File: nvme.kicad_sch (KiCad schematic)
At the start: 18 parts, among them J4 Bus_M.2_Socket_M, U7 ASEK-32.768KHZ-L-R-T, U8 AP3441SHE-7B

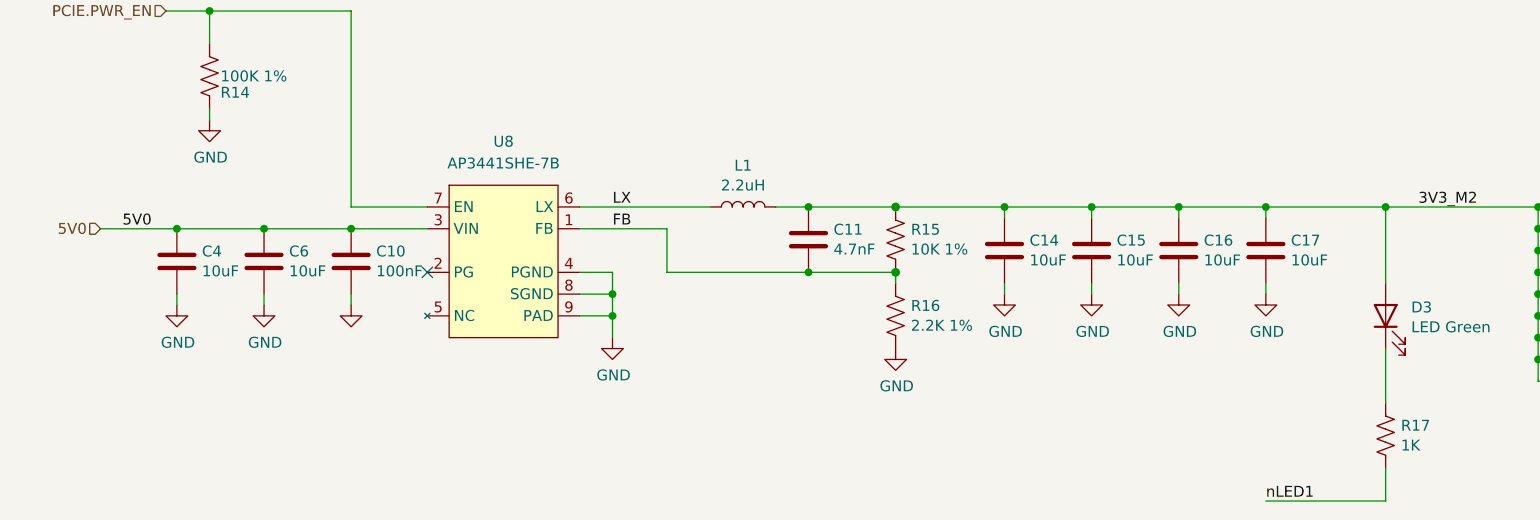
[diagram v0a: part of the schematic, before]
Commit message: restructured symbols, added footprints
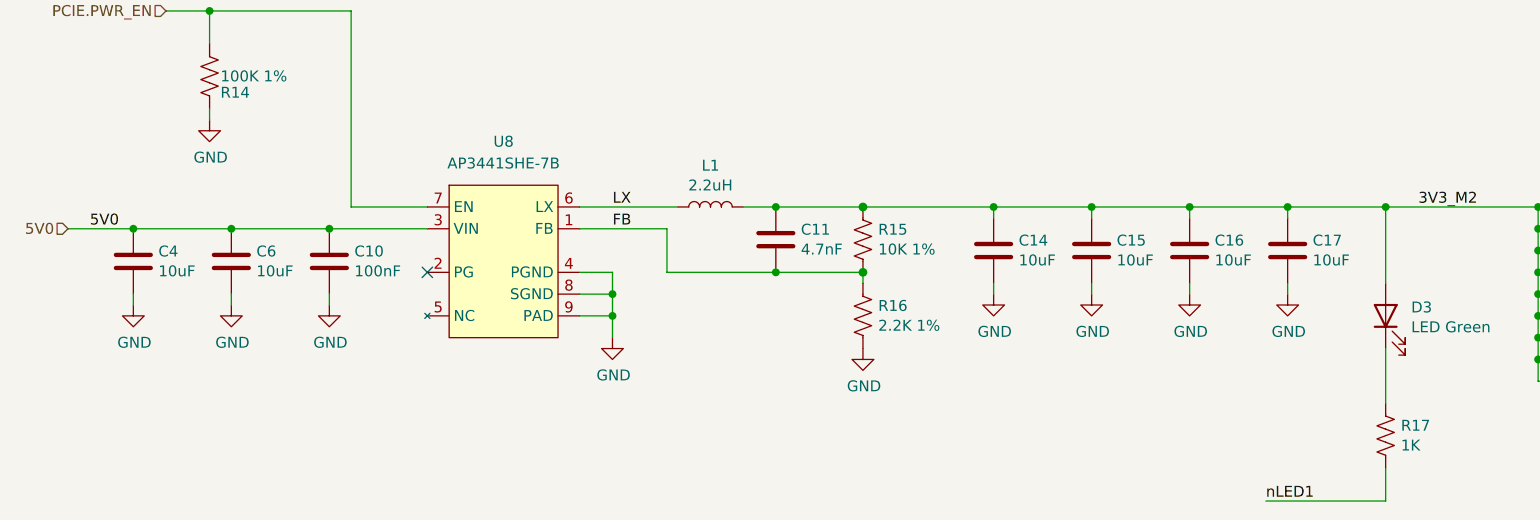
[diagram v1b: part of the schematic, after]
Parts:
- C10, C11, C14, C15, C16, C17, C19, C4, C6: symbol Device:C -> library:C
- D3: symbol Device:LED -> library:LED
- J4: symbol CM5IO:Bus_M.2_Socket_M -> library:Bus_M.2_Socket_M
- L1: symbol Device:L -> library:L
- R14, R15, R16, R17: symbol Device:R_US -> library:R_US
- U7: symbol CM5IO:ASEK-32.768KHZ-L-R-T -> library:ASEK-32.768KHZ-L-R-T
- U8: symbol CM5IO:AP3441SHE-7B -> library:AP3441SHE-7B
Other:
- moved on the sheet: C10, C11, C14, C16, C17, C4, C6, L1, R15, R16

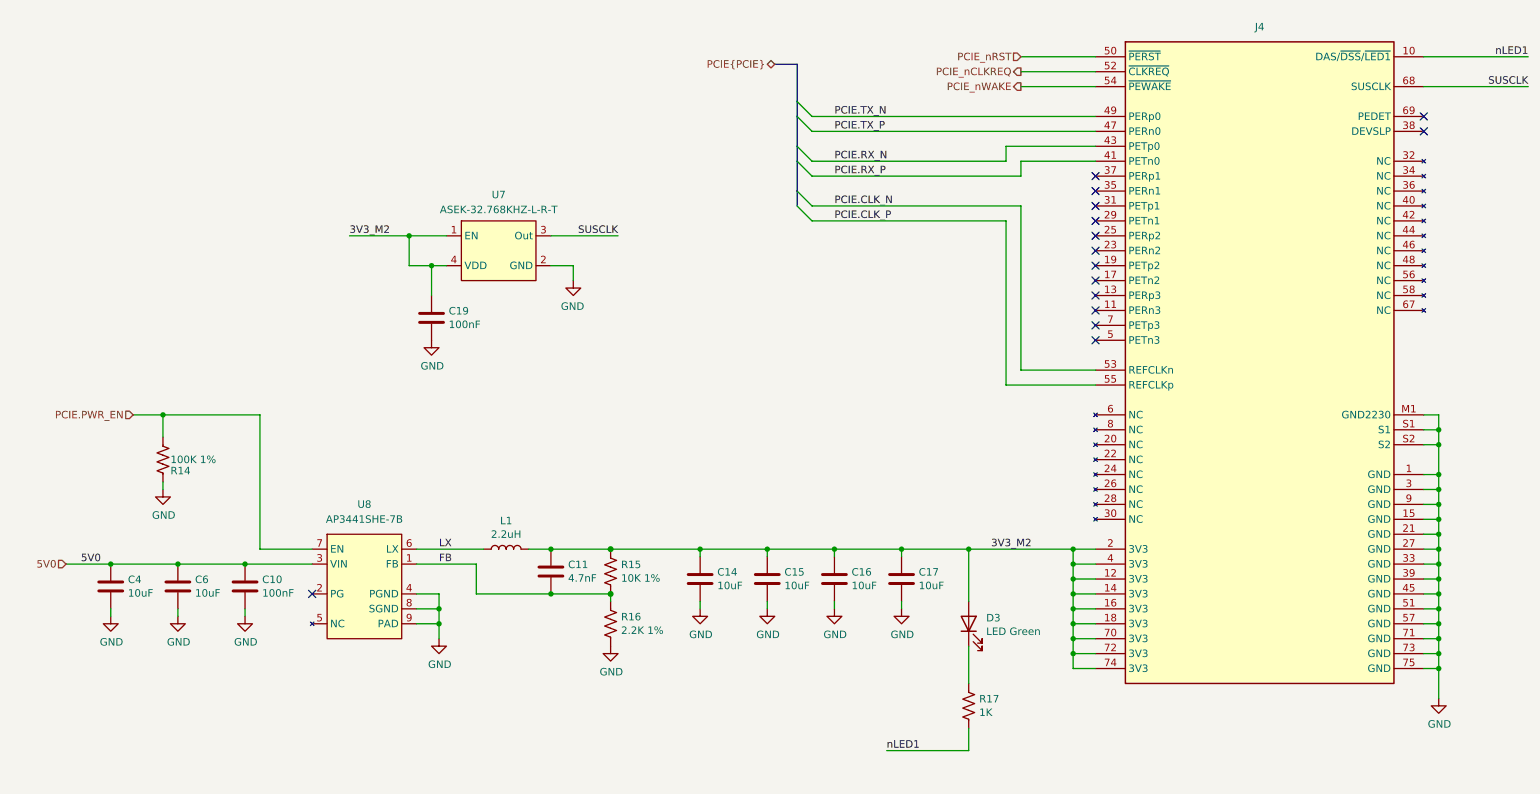
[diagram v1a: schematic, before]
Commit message: added second camera, 6-axis imu
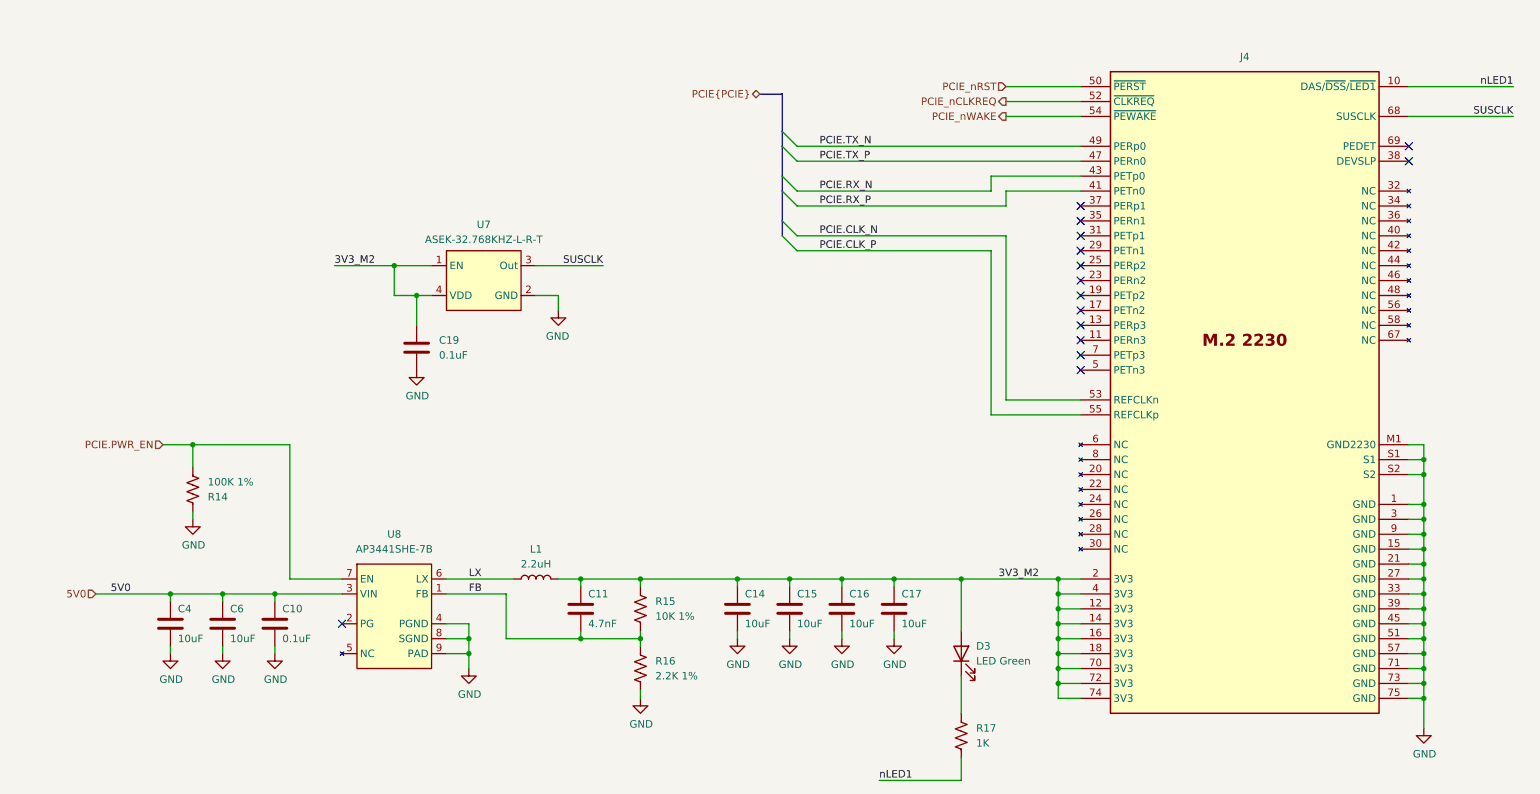
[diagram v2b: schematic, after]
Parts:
- C10, C19: value 100nF -> 0.1uF
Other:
- moved on the sheet: C10, C11, C14, C15, C16, C17, C19, C4, C6, D3, L1, R14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

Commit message: annotations, small fixes
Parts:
- renumbered C19 to C1, C11 to C2, C14 to C3, C15 to C4, C16 to C5, C17 to C6, C4 to C7, C6 to C8, C10 to C9, J4 to J3, R14 to R5, R15 to R6, R16 to R7, R17 to R8, U7 to U1, U8 to U2
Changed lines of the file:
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@@
 		(on_board yes)
 		(dnp no)
-		(property "Reference" "C16"
+		(property "Reference" "C5"
 			(at 157.48 123.19 0)
 			(effects
@@
 			(project "CUTIE-CITRUS"
 				(path "/40af415e-5e3a-41a5-ab07-08c2181863e4/7953df6c-8185-4fff-8cd2-b6d3791adbaa"
-					(reference "C16")
+					(reference "C5")
 					(unit 1)
 				)
@@
 		(on_board yes)
 		(dnp no)
-		(property "Reference" "#PWR018"
+		(property "Reference" "#PWR012"
 			(at 156.21 137.16 0)
 			(effects
@@
 			(project "CUTIE-CITRUS"
 				(path "/40af415e-5e3a-41a5-ab07-08c2181863e4/7953df6c-8185-4fff-8cd2-b6d3791adbaa"
-					(reference "#PWR018")
+					(reference "#PWR012")
 					(unit 1)
 				)
@@
 		(on_board yes)
 		(dnp no)
-		(property "Reference" "C6"
+		(property "Reference" "C8"
 			(at 52.07 125.73 0)
 			(effects
@@
 			(project "CUTIE-CITRUS"
 				(path "/40af415e-5e3a-41a5-ab07-08c2181863e4/7953df6c-8185-4fff-8cd2-b6d3791adbaa"
-					(reference "C6")
+					(reference "C8")
 					(unit 1)
 				)
@@
 		(on_board yes)
 		(dnp no)
-		(property "Reference" "#PWR021"
+		(property "Reference" "#PWR015"
 			(at 50.8 139.7 0)
 			(effects
@@
 			(project "CUTIE-CITRUS"
 				(path "/40af415e-5e3a-41a5-ab07-08c2181863e4/7953df6c-8185-4fff-8cd2-b6d3791adbaa"
-					(reference "#PWR021")
+					(reference "#PWR015")
 					(unit 1)
 				)
@@
 		(on_board yes)
 		(dnp no)
-		(property "Reference" "#PWR03"
+		(property "Reference" "#PWR019"
 			(at 255.27 152.4 0)
 			(effects
@@
 			(project "CUTIE-CITRUS"
 				(path "/40af415e-5e3a-41a5-ab07-08c2181863e4/7953df6c-8185-4fff-8cd2-b6d3791adbaa"
-					(reference "#PWR03")
+					(reference "#PWR019")
 					(unit 1)
 				)
@@
 		(on_board yes)
 		(dnp no)
-		(property "Reference" "#PWR024"
+		(property "Reference" "#PWR013"
 			(at 165.1 137.16 0)
 			(effects
@@
 			(project "CUTIE-CITRUS"
 				(path "/40af415e-5e3a-41a5-ab07-08c2181863e4/7953df6c-8185-4fff-8cd2-b6d3791adbaa"
-					(reference "#PWR024")
+					(reference "#PWR013")
 					(unit 1)
 				)
@@
 		(on_board yes)
 		(dnp no)
-		(property "Reference" "R17"
+		(property "Reference" "R8"
 			(at 179.07 146.05 0)
 			(effects
@@
 			(project "CUTIE-CITRUS"
 				(path "/40af415e-5e3a-41a5-ab07-08c2181863e4/7953df6c-8185-4fff-8cd2-b6d3791adbaa"
-					(reference "R17")
+					(reference "R8")
 					(unit 1)
 				)
@@
 		(on_board yes)
 		(dnp no)
-		(property "Reference" "R15"
+		(property "Reference" "R6"
 			(at 124.46 124.46 0)
 			(effects
@@
 			(project "CUTIE-CITRUS"
 				(path "/40af415e-5e3a-41a5-ab07-08c2181863e4/7953df6c-8185-4fff-8cd2-b6d3791adbaa"
-					(reference "R15")
+					(reference "R6")
 					(unit 1)
 				)
@@
 		(on_board yes)
 		(dnp no)
-		(property "Reference" "C19"
+		(property "Reference" "C1"
 			(at 87.63 80.01 0)
 			(effects
@@
 			(project "CUTIE-CITRUS"
 				(path "/40af415e-5e3a-41a5-ab07-08c2181863e4/7953df6c-8185-4fff-8cd2-b6d3791adbaa"
-					(reference "C19")
+					(reference "C1")
 					(unit 1)
 				)
@@
 		(on_board yes)
 		(dnp no)
-		(property "Reference" "R14"
+		(property "Reference" "R5"
 			(at 48.26 106.68 0)
 			(effects
@@
 			(project "CUTIE-CITRUS"
 				(path "/40af415e-5e3a-41a5-ab07-08c2181863e4/7953df6c-8185-4fff-8cd2-b6d3791adbaa"
-					(reference "R14")
+					(reference "R5")
 					(unit 1)
 				)
@@
 		(on_board yes)
 		(dnp no)
-		(property "Reference" "R16"
+		(property "Reference" "R7"
 			(at 124.46 134.62 0)
 			(effects
@@
 			(project "CUTIE-CITRUS"
 				(path "/40af415e-5e3a-41a5-ab07-08c2181863e4/7953df6c-8185-4fff-8cd2-b6d3791adbaa"
-					(reference "R16")
+					(reference "R7")
 					(unit 1)
 				)
@@
 		(dnp no)
 		(fields_autoplaced yes)
-		(property "Reference" "U7"
+		(property "Reference" "U1"
 			(at 95.25 60.325 0)
 			(effects
@@
 			(project "CUTIE-CITRUS"
 				(path "/40af415e-5e3a-41a5-ab07-08c2181863e4/7953df6c-8185-4fff-8cd2-b6d3791adbaa"
-					(reference "U7")
+					(reference "U1")
 					(unit 1)
 				)
@@
 		(on_board yes)
 		(dnp no)
-		(property "Reference" "C4"
+		(property "Reference" "C7"
 			(at 43.18 125.73 0)
 			(effects
@@
 			(project "CUTIE-CITRUS"
 				(path "/40af415e-5e3a-41a5-ab07-08c2181863e4/7953df6c-8185-4fff-8cd2-b6d3791adbaa"
-					(reference "C4")
+					(reference "C7")
 					(unit 1)
 				)
@@
 		(dnp no)
 		(fields_autoplaced yes)
-		(property "Reference" "U8"
+		(property "Reference" "U2"
 			(at 80.01 113.03 0)
 			(effects
@@
 			(project "CUTIE-CITRUS"
 				(path "/40af415e-5e3a-41a5-ab07-08c2181863e4/7953df6c-8185-4fff-8cd2-b6d3791adbaa"
-					(reference "U8")
+					(reference "U2")
 					(unit 1)
 				)
@@
 		(on_board yes)
 		(dnp no)
-		(property "Reference" "C10"
+		(property "Reference" "C9"
 			(at 60.96 125.73 0)
 			(effects
@@
 			(project "CUTIE-CITRUS"
 				(path "/40af415e-5e3a-41a5-ab07-08c2181863e4/7953df6c-8185-4fff-8cd2-b6d3791adbaa"
-					(reference "C10")
+					(reference "C9")
 					(unit 1)
 				)
@@
 		(on_board yes)
 		(dnp no)
-		(property "Reference" "C14"
+		(property "Reference" "C3"
 			(at 139.7 123.19 0)
 			(effects
@@
 			(project "CUTIE-CITRUS"
 				(path "/40af415e-5e3a-41a5-ab07-08c2181863e4/7953df6c-8185-4fff-8cd2-b6d3791adbaa"
-					(reference "C14")
+					(reference "C3")
 					(unit 1)
 				)
@@
 		(on_board yes)
 		(dnp no)
-		(property "Reference" "#PWR020"
+		(property "Reference" "#PWR014"
 			(at 41.91 139.7 0)
 			(effects
@@
 			(project "CUTIE-CITRUS"
 				(path "/40af415e-5e3a-41a5-ab07-08c2181863e4/7953df6c-8185-4fff-8cd2-b6d3791adbaa"
-					(reference "#PWR020")
+					(reference "#PWR014")
 					(unit 1)
 				)
@@
 		(on_board yes)
 		(dnp no)
-		(property "Reference" "#PWR08"
+		(property "Reference" "#PWR09"
 			(at 45.72 116.84 0)
 			(effects
@@
 			(project "CUTIE-CITRUS"
 				(path "/40af415e-5e3a-41a5-ab07-08c2181863e4/7953df6c-8185-4fff-8cd2-b6d3791adbaa"
-					(reference "#PWR08")
+					(reference "#PWR09")
 					(unit 1)
 				)
@@
 		(on_board yes)
 		(dnp no)
-		(property "Reference" "#PWR016"
+		(property "Reference" "#PWR018"
 			(at 121.92 147.32 0)
 			(effects
@@
 			(project "CUTIE-CITRUS"
 				(path "/40af415e-5e3a-41a5-ab07-08c2181863e4/7953df6c-8185-4fff-8cd2-b6d3791adbaa"
-					(reference "#PWR016")
+					(reference "#PWR018")
 					(unit 1)
 				)
@@
 		(on_board yes)
 		(dnp no)
-		(property "Reference" "#PWR04"
+		(property "Reference" "#PWR016"
 			(at 59.69 139.7 0)
 			(effects
@@
 			(project "CUTIE-CITRUS"
 				(path "/40af415e-5e3a-41a5-ab07-08c2181863e4/7953df6c-8185-4fff-8cd2-b6d3791adbaa"
-					(reference "#PWR04")
+					(reference "#PWR016")
 					(unit 1)
 				)
@@
 		(on_board yes)
 		(dnp no)
-		(property "Reference" "C11"
+		(property "Reference" "C2"
 			(at 113.03 123.19 0)
 			(effects
@@
 			(project "CUTIE-CITRUS"
 				(path "/40af415e-5e3a-41a5-ab07-08c2181863e4/7953df6c-8185-4fff-8cd2-b6d3791adbaa"
-					(reference "C11")
+					(reference "C2")
 					(unit 1)
 				)
@@
 		(on_board yes)
 		(dnp no)
-		(property "Reference" "#PWR015"
+		(property "Reference" "#PWR011"
 			(at 147.32 137.16 0)
 			(effects
@@
 			(project "CUTIE-CITRUS"
 				(path "/40af415e-5e3a-41a5-ab07-08c2181863e4/7953df6c-8185-4fff-8cd2-b6d3791adbaa"
-					(reference "#PWR015")
+					(reference "#PWR011")
 					(unit 1)
 				)
@@
 		(on_board yes)
 		(dnp no)
-		(property "Reference" "#PWR028"
+		(property "Reference" "#PWR017"
 			(at 92.71 142.24 0)
 			(effects
@@
 			(project "CUTIE-CITRUS"
 				(path "/40af415e-5e3a-41a5-ab07-08c2181863e4/7953df6c-8185-4fff-8cd2-b6d3791adbaa"
-					(reference "#PWR028")
+					(reference "#PWR017")
 					(unit 1)
 				)
@@
 		(on_board yes)
 		(dnp no)
-		(property "Reference" "C15"
+		(property "Reference" "C4"
 			(at 148.59 123.19 0)
 			(effects
@@
 			(project "CUTIE-CITRUS"
 				(path "/40af415e-5e3a-41a5-ab07-08c2181863e4/7953df6c-8185-4fff-8cd2-b6d3791adbaa"
-					(reference "C15")
+					(reference "C4")
 					(unit 1)
 				)
@@
 		(on_board yes)
 		(dnp no)
-		(property "Reference" "#PWR025"
+		(property "Reference" "#PWR08"
 			(at 83.82 91.44 0)
 			(effects
@@
 			(project "CUTIE-CITRUS"
 				(path "/40af415e-5e3a-41a5-ab07-08c2181863e4/7953df6c-8185-4fff-8cd2-b6d3791adbaa"
-					(reference "#PWR025")
+					(reference "#PWR08")
 					(unit 1)
 				)
@@
 		(on_board yes)
 		(dnp no)
-		(property "Reference" "J4"
+		(property "Reference" "J3"
 			(at 224.79 31.75 0)
 			(effects
@@
 			(project "CUTIE-CITRUS"
 				(path "/40af415e-5e3a-41a5-ab07-08c2181863e4/7953df6c-8185-4fff-8cd2-b6d3791adbaa"
-					(reference "J4")
+					(reference "J3")
 					(unit 1)
 				)
@@
 		(on_board yes)
 		(dnp no)
-		(property "Reference" "C17"
+		(property "Reference" "C6"
 			(at 166.37 123.19 0)
 			(effects
@@
 			(project "CUTIE-CITRUS"
 				(path "/40af415e-5e3a-41a5-ab07-08c2181863e4/7953df6c-8185-4fff-8cd2-b6d3791adbaa"
-					(reference "C17")
+					(reference "C6")
 					(unit 1)
 				)
@@
 		(on_board yes)
 		(dnp no)
-		(property "Reference" "#PWR026"
+		(property "Reference" "#PWR07"
 			(at 107.95 81.28 0)
 			(effects
@@
 			(project "CUTIE-CITRUS"
 				(path "/40af415e-5e3a-41a5-ab07-08c2181863e4/7953df6c-8185-4fff-8cd2-b6d3791adbaa"
-					(reference "#PWR026")
+					(reference "#PWR07")
 					(unit 1)
 				)
@@
 		(on_board yes)
 		(dnp no)
-		(property "Reference" "#PWR017"
+		(property "Reference" "#PWR010"
 			(at 138.43 137.16 0)
 			(effects
@@
 			(project "CUTIE-CITRUS"
 				(path "/40af415e-5e3a-41a5-ab07-08c2181863e4/7953df6c-8185-4fff-8cd2-b6d3791adbaa"
-					(reference "#PWR017")
-					(unit 1)
-				)
+					(reference "#PWR010")
+					(unit 1)
+				)

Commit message: extra abstraction layer for cm5 conns.
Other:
- company: (none) -> Andre S Winkel | Highlander Space Program | University of California, Riverside
- title: (none) -> CUTIE-CITRUS PCB
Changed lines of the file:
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@@
 	(generator_version "9.0")
 	(paper "A4")
+	(title_block
+		(title "CUTIE-CITRUS PCB")
+		(date "2025-11-24")
+		(rev "A")
+		(company "Andre S Winkel | Highlander Space Program | University of California, Riverside")
+	)
 	(junction
 		(at 80.01 67.31)
